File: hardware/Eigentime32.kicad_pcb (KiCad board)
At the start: 2 copper layers, 40 x 40 mm, 0 parts

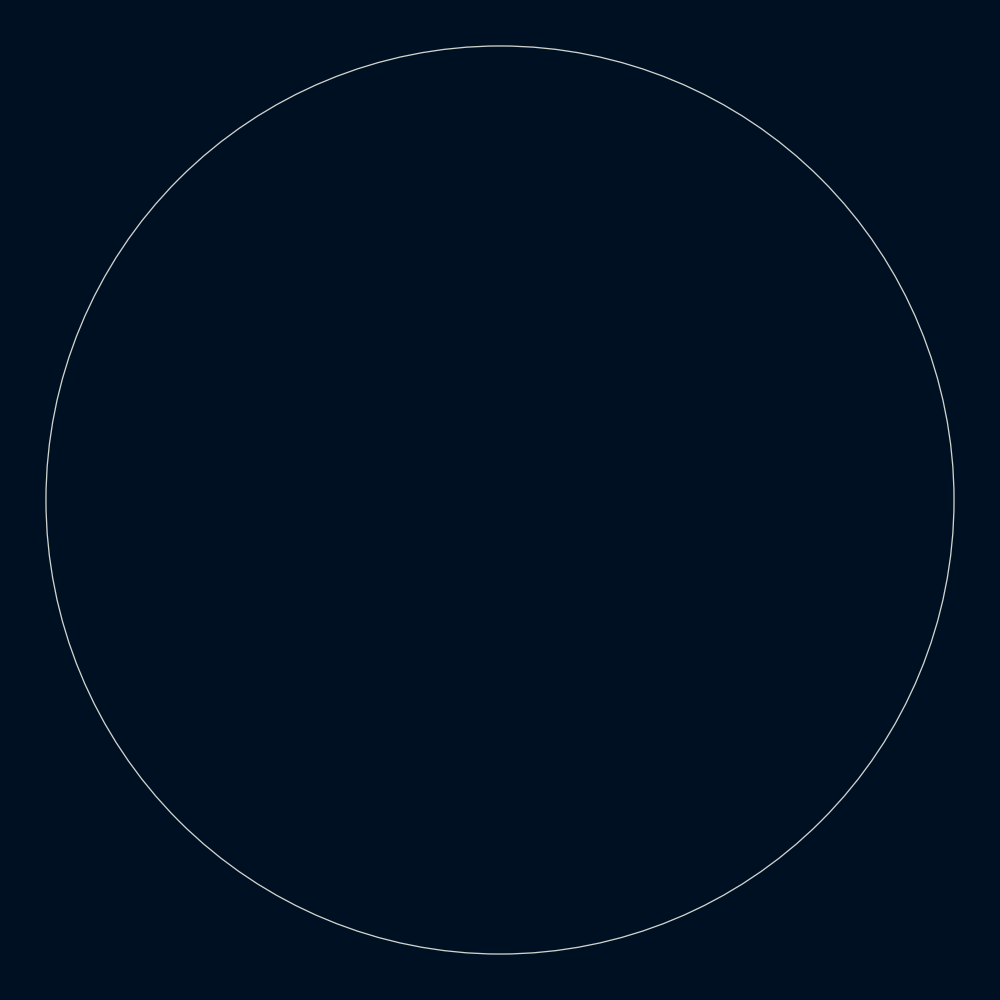
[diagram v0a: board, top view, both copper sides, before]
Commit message: Layout phase 1: placement, NFC coil, part picks for TBD footprints
Board: 40 mm round, 0.8 mm, 2 layers. Front carries only the NFC coil
(LCD keep-out rule area); every other part is on the back around the
centred CR2032 holder (nothing taller than its 4.06 mm). Buttons at
12 o'clock, hinge mark at 9, lid sensor at 3, LCD FPC connector at 6.
Rules: 0.15 mm clearance, 0.2 mm tracks, 0.5/0.3 mm vias, 0.3 mm
copper-to-edge. A rule area forbids copper pour anywhere inside the
coil. Reference designators are on the fab layers.

NFC coil: 8-turn Archimedean spiral on F.Cu, 38.1 mm OD, 0.15/0.15 mm,
built as one polygon in a net-tie footprint (AE1) with plated terminal
vias at 4-5 o'clock next to U8.

Parts: lid sensor is now an Allegro CT8132SK-IS3 TMR switch (push-pull,
no pull-up; SMD NC reeds don't fit and the Coto RR122 is obsolete);
buttons are Panasonic EVQ-P7A01P side-push switches. MCU sheet, BOM
and docs updated. KiCad-written project defaults in .kicad_pro are
included.

ERC clean; DRC: 0 violations, 0 parity issues, only unrouted nets.
Renders in docs/renders.

Co-Authored-By: Claude Opus 5.5 (1M context) <noreply@anthropic.com>
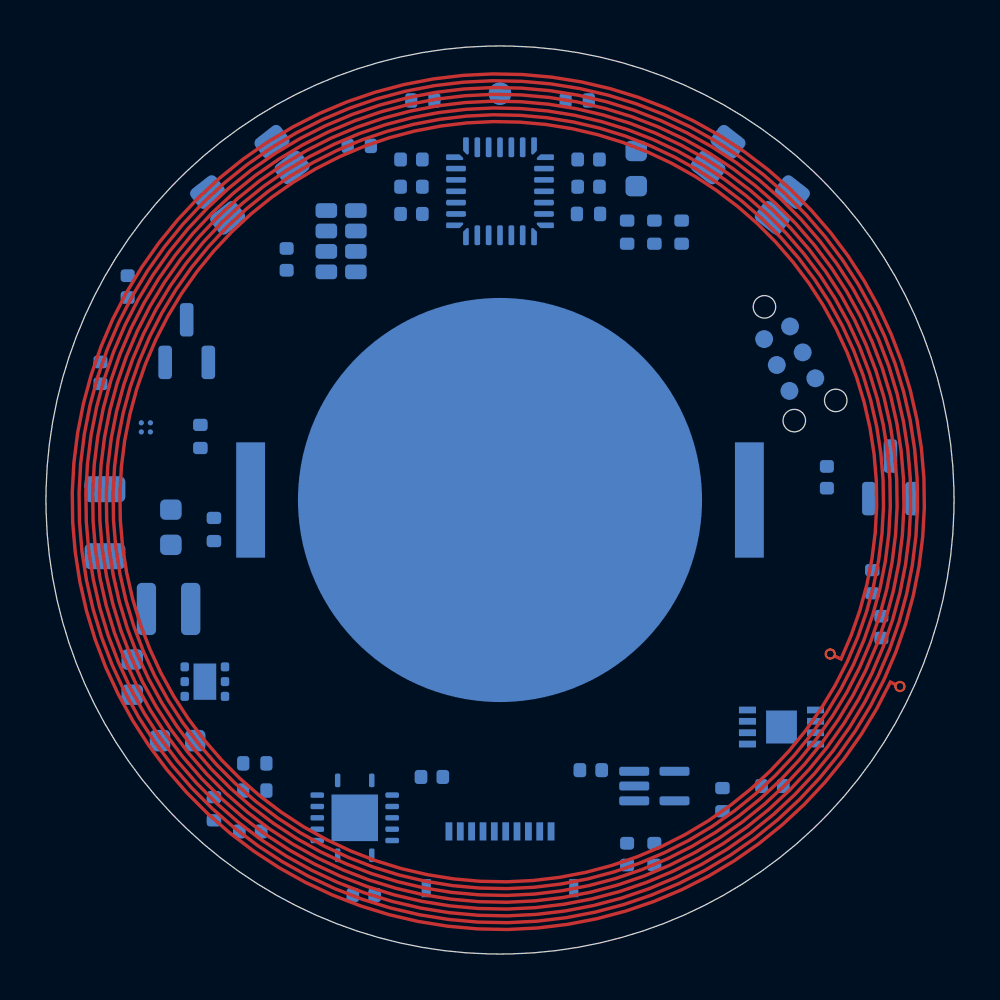
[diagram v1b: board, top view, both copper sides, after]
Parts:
- added AE1: NFC coil, Eigentime32:NFC_PCB_Coil_D38.1mm_8T, F.Cu at (148.5, 105.0)
- added BT1: CR2032, Battery:BatteryHolder_Keystone_3034_1x20mm, B.Cu at (148.5, 105.0)
- added C10: 100n, Capacitor_SMD:C_0402_1005Metric, B.Cu at (144.6, 90.0)
- added C11: 100n, Capacitor_SMD:C_0402_1005Metric, B.Cu at (152.4, 90.0)
- added C12: 100n, Capacitor_SMD:C_0402_1005Metric, B.Cu at (144.6, 91.2)
- added C13: 1u, Capacitor_SMD:C_0402_1005Metric, B.Cu at (144.6, 92.4)
- added C14: 10u, Capacitor_SMD:C_0603_1608Metric, B.Cu at (154.5, 90.4)
- added C15: 100n, Capacitor_SMD:C_0402_1005Metric, B.Cu at (152.4, 91.2)
- added C16: 100n, Capacitor_SMD:C_0402_1005Metric, B.Cu at (145.5, 117.2)
- added C17: 100n, Capacitor_SMD:C_0402_1005Metric, B.Cu at (152.5, 116.9)
- added C18: 1u, Capacitor_SMD:C_0402_1005Metric, B.Cu at (154.1, 120.6)
- added C19: 1u, Capacitor_SMD:C_0402_1005Metric, B.Cu at (155.3, 120.6)
- added C2: 100u, Capacitor_SMD:C_1206_3216Metric, B.Cu at (131.1, 106.0)
- added C20: 100n, Capacitor_SMD:C_0402_1005Metric, B.Cu at (142.5, 122.4)
- added C21: 100n, Capacitor_SMD:C_0402_1005Metric, B.Cu at (160.5, 117.6)
- added C22: DNP, Capacitor_SMD:C_0402_1005Metric, B.Cu at (165.3, 110.6)
- added C23: 1u, Capacitor_SMD:C_0402_1005Metric, B.Cu at (162.9, 104.0)
- added C3: 100n, Capacitor_SMD:C_0402_1005Metric, B.Cu at (132.1, 95.6)
- added C4: 10u, Capacitor_SMD:C_0603_1608Metric, B.Cu at (134.0, 106.2)
- added C5: 10u, Capacitor_SMD:C_0603_1608Metric, B.Cu at (132.3, 112.8)
- added C6: 10u, Capacitor_SMD:C_0603_1608Metric, B.Cu at (134.3, 115.6)
- added C7: 1u, Capacitor_SMD:C_0402_1005Metric, B.Cu at (130.9, 99.4)
- added C8: 470n, Capacitor_SMD:C_0402_1005Metric, B.Cu at (137.5, 119.6)
- added C9: 100n, Capacitor_SMD:C_0402_1005Metric, B.Cu at (139.1, 94.4)
- added J1: TC2030-NL, Connector:Tag-Connect_TC2030-IDC-NL_2x03_P1.27mm_Vertical, B.Cu at (161.3, 98.8)
- added J2: AYF531035, Eigentime32:Panasonic_AYF531035_1x10-1MP_P0.5mm_Horizontal, B.Cu at (148.5, 119.6)
- added L1: 1u, Inductor_SMD:L_Wuerth_MAPI-2512, B.Cu at (133.9, 109.8)
- added Q1: DMG2305UX, Package_TO_SOT_SMD:SOT-23, B.Cu at (134.7, 98.0)
- added R1: 402k, Resistor_SMD:R_0402_1005Metric, B.Cu at (137.7, 116.6)
- added R10: 10k, Resistor_SMD:R_0402_1005Metric, B.Cu at (152.4, 92.4)
- added R12: 1M, Resistor_SMD:R_0402_1005Metric, B.Cu at (145.1, 87.4)
- added R13: 1M, Resistor_SMD:R_0402_1005Metric, B.Cu at (151.9, 87.4)
- added R14: 1M, Resistor_SMD:R_0402_1005Metric, B.Cu at (164.9, 108.6)
- added R15: 100k, Resistor_SMD:R_0402_1005Metric, B.Cu at (158.3, 118.2)
- added R2: 200k, Resistor_SMD:R_0402_1005Metric, B.Cu at (137.7, 117.8)
- added R3: 1M, Resistor_SMD:R_0402_1005Metric, B.Cu at (135.9, 106.3)
- added R4: 470, Resistor_SMD:R_0402_1005Metric, B.Cu at (135.3, 102.2)
- added R5: 1M, Resistor_SMD:R_0402_1005Metric, B.Cu at (135.9, 118.6)
- added R6: 10k, Resistor_SMD:R_0402_1005Metric, B.Cu at (155.3, 93.2)
- added R7: 10k, Resistor_SMD:R_0402_1005Metric, B.Cu at (156.5, 93.2)
- added R8: 470k, Resistor_SMD:R_0402_1005Metric, B.Cu at (154.1, 93.2)
- added R9: 10k, Resistor_SMD:R_0402_1005Metric, B.Cu at (142.3, 89.4)
- added SW2: BTN1, Button_Switch_SMD:SW_SPST_EVQP7A, B.Cu at (137.5, 90.9)
- added SW3: BTN2, Button_Switch_SMD:SW_SPST_EVQP7A, B.Cu at (159.5, 90.9)
- added TP1: CLKOUT, TestPoint:TestPoint_Pad_D1.0mm, B.Cu at (148.5, 87.1)
- added U1: RV-3032-C7, Package_SON:MicroCrystal_C7_SON-8_1.5x3.2mm_P0.9mm, B.Cu at (141.5, 93.6)
- added U2: STM32L031G6U6, Package_DFN_QFN:QFN-28_4x4mm_P0.5mm, B.Cu at (148.5, 91.4)
- added U3: TPS61099DRV, Package_SON:WSON-6-1EP_2x2mm_P0.65mm_EP1x1.6mm, B.Cu at (135.5, 113.0)
- added U5: TPS22916C, Package_BGA:Texas_PicoStar_BGA-4_0.758x0.758mm_Layout2x2_P0.4mm, B.Cu at (132.9, 101.8)
- added U6: SN74LV4T125, Eigentime32:Texas_RGY0014A_VQFN-14-1EP_3.5x3.5mm_P0.5mm_EP2.05x2.05mm, B.Cu at (142.1, 119.0)
- added U7: SN74LV1T34, Package_TO_SOT_SMD:SOT-353_SC-70-5, B.Cu at (155.3, 117.6)
- added U8: ST25DV04KC-IE6C3, Package_DFN_QFN:DFN-8-1EP_3x2mm_P0.5mm_EP1.36x1.46mm, B.Cu at (160.9, 115.0)
- added U9: CT8132SK-IS3, Package_TO_SOT_SMD:SOT-23, B.Cu at (165.7, 104.0)
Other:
- board text added: "BUTTONS"
- board text added: "HINGE"
- board text added: "LCD 26.6 x 30.3 (front), FPC ledge at 6 o'clock"
- board text added: "LCD FPC"
- board text added: "LID MAGNET"

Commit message: Layout: re-place parts around the CR2032 insertion channel
The Keystone 3034 is a tunnel retainer: the cell slides in flat from
12 o'clock with ~0.5 mm headroom, so a 21 mm wide path from the holder
to the board edge must be free of parts. A back-side rule area now
keeps it clear. The MCU, RTC and buttons moved out of it: MCU and RTC
on the right, buttons at ~10 and ~2 o'clock, lid sensor at ~4, SWD
pads at ~7:30, power on the left.

The TC2030 footprint is a project copy whose small via keep-out allows
nearby footprints (KiCad checks footprint keep-outs against bounding
boxes, and the holder's box covered it).

DRC: 0 violations, 0 parity issues; nets still unrouted.

Co-Authored-By: Claude Opus 5.5 (1M context) <noreply@anthropic.com>
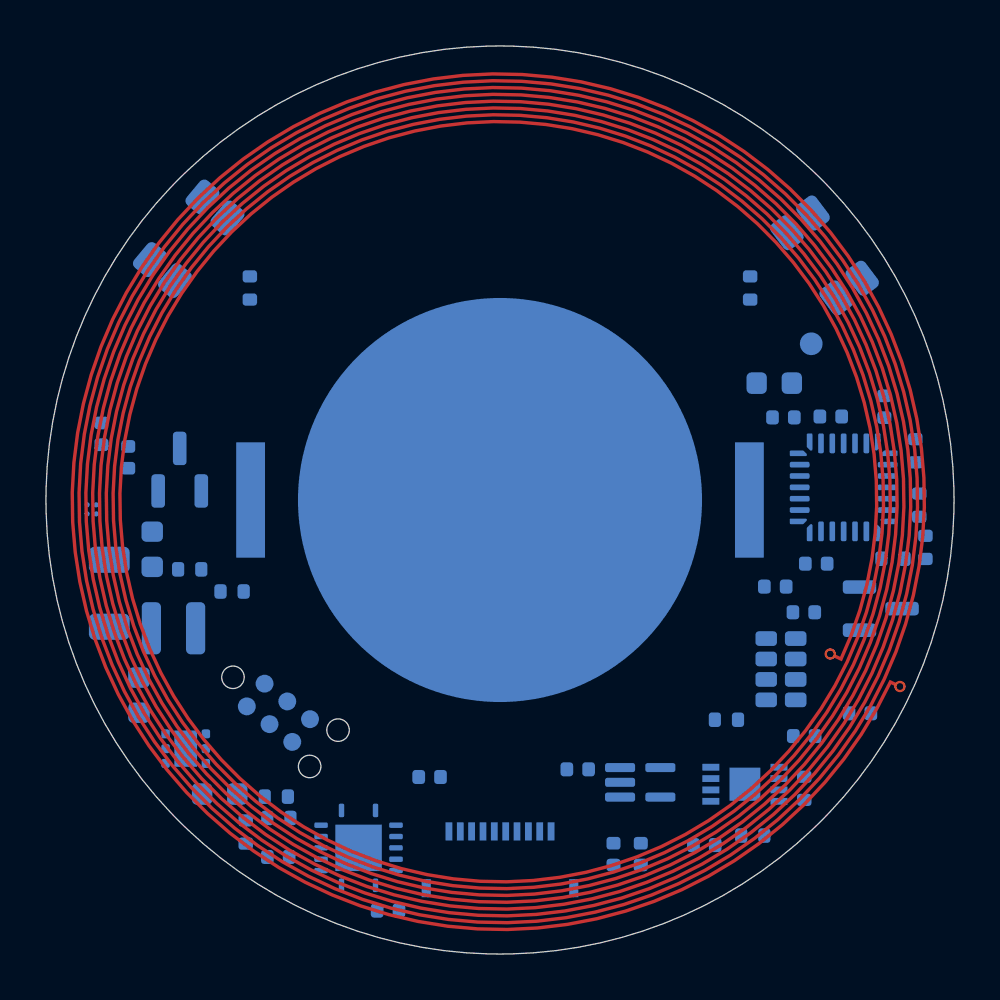
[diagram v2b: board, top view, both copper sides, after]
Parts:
- J1: footprint Connector:Tag-Connect_TC2030-IDC-NL_2x03_P1.27mm_Vertical -> Eigentime32:Tag-Connect_TC2030-IDC-NL_2x03_P1.27mm_Vertical_FootprintsAllowed
- moved R9 30.0 mm to (158.5, 114.7)
- moved C9 27.6 mm to (161.9, 109.9), turned to 0 degrees
- moved J1 27.4 mm to (138.7, 114.4), turned to -38 degrees
- moved U1 27.0 mm to (160.9, 112.5)
- moved C13 22.5 mm to (165.4, 100.9), turned to 90 degrees
- moved C12 21.1 mm to (163.1, 101.3)
- moved C11 20.5 mm to (160.6, 108.8)
- moved R10 20.3 mm to (165.8, 107.6)
- moved U2 20.0 mm to (163.6, 104.4)
- moved C10 19.9 mm to (161.0, 101.4)
- moved C15 19.4 mm to (162.4, 107.8)
- moved R6 18.3 mm to (167.2, 107.1)
- moved TP1 17.6 mm to (162.2, 98.1)
- moved R7 15.9 mm to (167.0, 105.2)
- moved R8 15.9 mm to (166.8, 102.8)
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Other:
- board text added: "CR2032 IN (slide from 12 o'clock)"

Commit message: Layout: MCU to 4:30, smaller cell pad, routing rules (unrouted)
Placement reworked for routability: the MCU moves to the widest part
of the ring at ~4:30, with NFC, RTC and lid sensor in the 3 o'clock
strip. The CR2032 negative pad is now 5 mm (project footprint; Keystone
asks for 3.96 mm square minimum) so tracks can run under the cell.

Routing rules are set but the board is not routed yet: 0.127 mm
clearance, 0.2 mm signal and 0.25 mm power tracks (Power netclass),
0.5/0.3 mm vias, 0.2 mm hole-to-copper, and a coil-ring keep-out (no
front tracks or vias between r 16.4 and 19.1 mm).

Freerouting 2.4.1 reaches ~20 of 143 connections unrouted on this
2-layer placement. ERC clean; DRC: 0 violations, 0 parity issues,
143 unrouted.

Co-Authored-By: Claude Opus 5.5 (1M context) <noreply@anthropic.com>
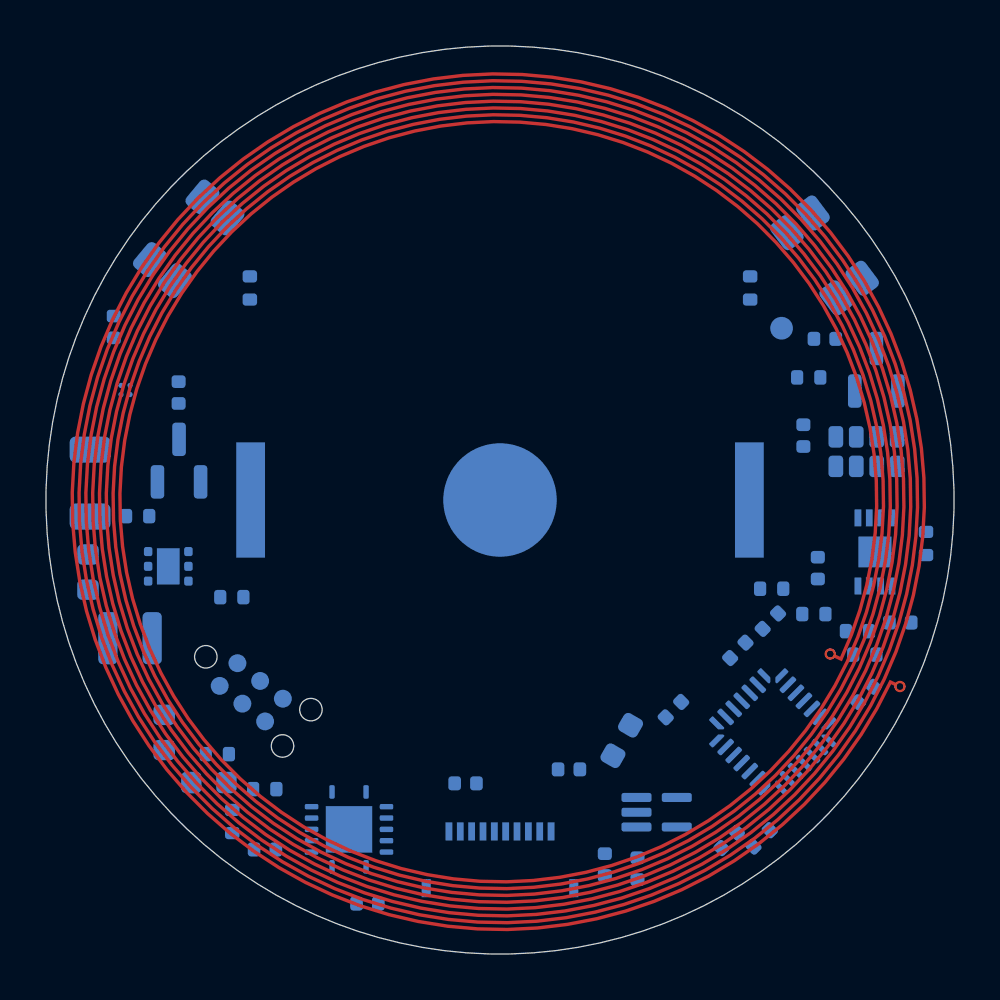
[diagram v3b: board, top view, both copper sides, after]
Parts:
- BT1: footprint Battery:BatteryHolder_Keystone_3034_1x20mm -> Eigentime32:BatteryHolder_Keystone_3034_1x20mm_SmallNegPad
- moved C13 20.3 mm to (158.6, 120.0), turned to 45 degrees
- moved C14 17.1 mm to (153.9, 115.6), turned to 60 degrees
- moved C23 16.6 mm to (162.8, 97.9)
- moved R9 15.5 mm to (162.1, 99.6)
- moved R15 15.0 mm to (167.3, 106.9), turned to 90 degrees
- moved C10 13.8 mm to (156.1, 114.2), turned to 45 degrees
- moved R10 13.6 mm to (160.0, 119.9), turned to 45 degrees
- moved C21 13.2 mm to (162.5, 108.0), turned to 90 degrees
- moved U8 11.7 mm to (165.0, 107.3), turned to 90 degrees
- moved U2 11.2 mm to (160.5, 115.2), turned to 45 degrees
- moved U9 10.5 mm to (165.1, 99.3), turned to 90 degrees
- moved U1 10.3 mm to (164.6, 102.9), turned to 90 degrees
- moved C12 9.40 mm to (160.4, 110.3), turned to 45 degrees
- moved R8 8.77 mm to (160.5, 108.9), turned to 0 degrees
- moved U3 8.07 mm to (133.9, 107.9)
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
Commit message: WIP layout-4l: 4-layer JLC04081H-3313 stackup, Freerouting pass
0.8 mm 4-layer stackup, In1/In2 as signal layers, no pours. Coil ring
keep-out on F/In1/In2. Freerouting result imported; 12 connections
still unrouted (being finished by hand/rip-up).

Co-Authored-By: Claude Opus 5.5 (1M context) <noreply@anthropic.com>
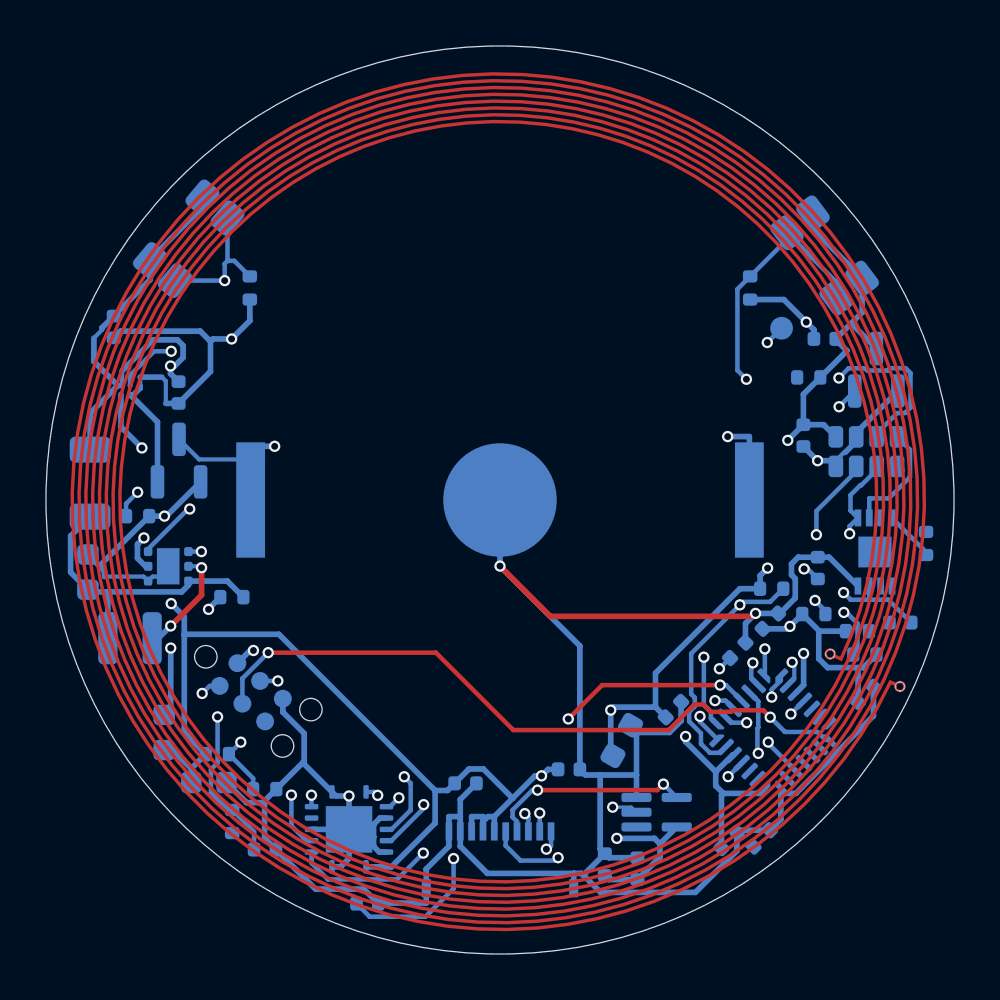
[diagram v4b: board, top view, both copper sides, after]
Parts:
- turned SW2 to 49.999 degrees
- turned SW3 to -53.002 degrees
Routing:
- net GND: track 0.00 -> 201.2 mm, vias 0 -> 8
- net /VBAT: track 0.00 -> 116.7 mm, vias 0 -> 9
- net /VLCD: track 0.00 -> 56.6 mm, vias 0 -> 4
- net /MCU/BTN1_N: track 0.00 -> 47.3 mm, vias 0 -> 2
- net /LCD_PWR_EN: track 0.00 -> 41.0 mm, vias 0 -> 3
- net /RTC_CLKOUT: track 0.00 -> 36.2 mm, vias 0 -> 3
- net /Power/VBAT_RAW: track 0.00 -> 30.5 mm, vias 0 -> 2
- net /MCU/NRST: track 0.00 -> 30.1 mm, vias 0 -> 3
- net /MCU/SWCLK: track 0.00 -> 30.0 mm, vias 0 -> 2
- net /MCU/BTN2_N: track 0.00 -> 27.5 mm, vias 0 -> 2
- net /LCD_SCLK: track 0.00 -> 25.3 mm, vias 0 -> 3
- net /LCD/DISP: track 0.00 -> 22.0 mm, vias 0 -> 3
- net /LCD_DISP: track 0.00 -> 20.9 mm, vias 0 -> 2
- net /Power/FB: track 0.00 -> 20.1 mm, vias 0 -> 2
- net /RTC_INT: track 0.00 -> 19.3 mm, vias 0 -> 2
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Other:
- copper layers 2 -> 4
